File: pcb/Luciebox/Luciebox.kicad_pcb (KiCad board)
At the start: 2 copper layers, 100 x 100 mm, 83 parts, among them J1 Screw_Terminal_01x07, J2 Screw_Terminal_01x07, J3 Screw_Terminal_01x07, J4 Screw_Terminal_01x07, J5 Screw_Terminal_01x07, P1 CONN_01X01, P2 CONN_01X01, P3 CONN_01X01, P4 CONN_01X01, P5 Digital, P6 Power, P7 Digital, P8 Analog, Q1 BC558, Q2 N-Channel_Mosfet, T1 terminal_13x1, T10 terminal_8x1, T11 terminal_3x1, T2 terminal_8x1, T3 terminal_8x1, T4 terminal_8x1, T5 terminal_8x1, T6 terminal_8x1, T7 terminal_8x1, T8 terminal_8x1, T9 terminal_8x1, U1 CA56-12SRWA, U2 ULN2003A, U3 ATmega328-PU, Y1 16MHz

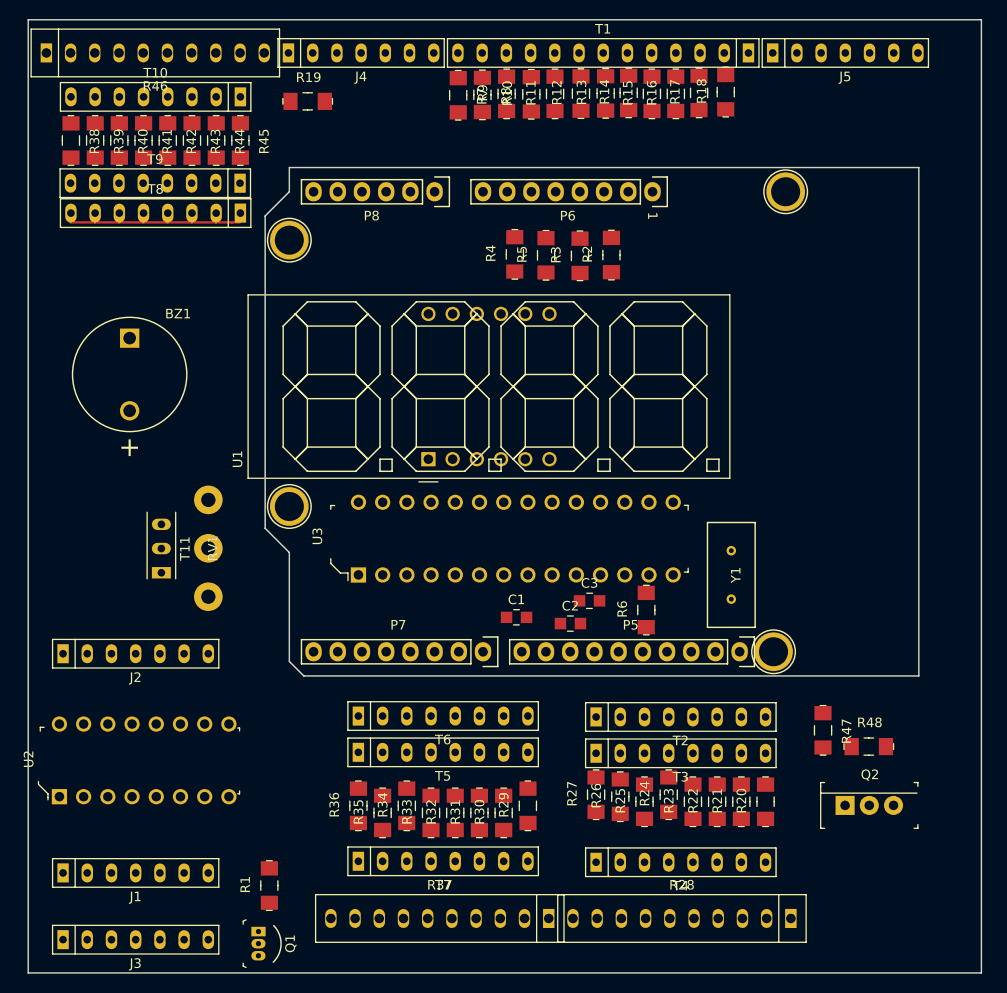
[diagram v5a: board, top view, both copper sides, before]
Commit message: pcb arrange components to input and ouput regions
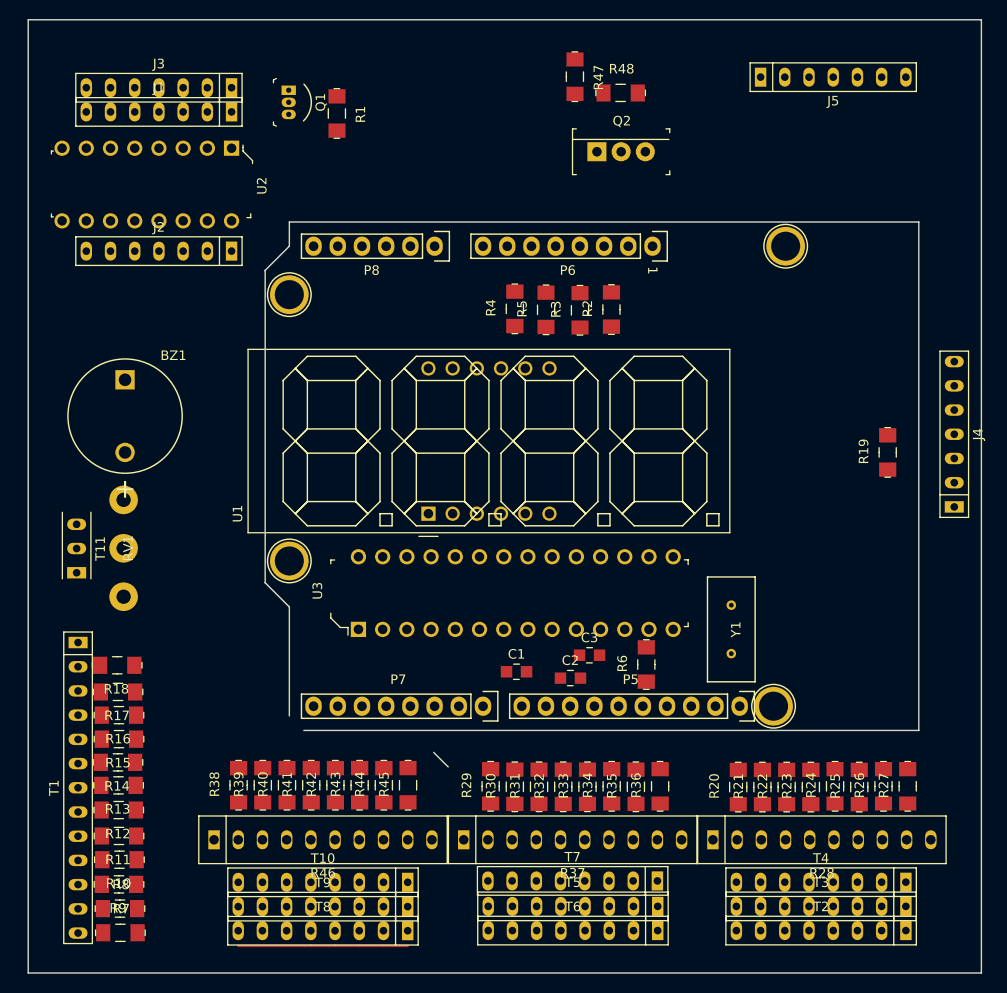
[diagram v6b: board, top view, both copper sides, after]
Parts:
- moved T1 94.8 mm to (85.2, 130.6), turned to 270 degrees
- moved R7 94.7 mm to (89.7, 145.8), turned to 0 degrees
- moved R8 93.5 mm to (89.6, 143.2), turned to 0 degrees
- moved R9 92.4 mm to (89.5, 140.7), turned to 180 degrees
- moved R10 91.2 mm to (89.6, 138.1), turned to 180 degrees
- moved R11 90.3 mm to (89.5, 135.6), turned to 180 degrees
- moved R12 89.5 mm to (89.5, 132.9), turned to 180 degrees
- moved J3 89.4 mm to (93.7, 57.1), turned to 180 degrees
- moved R13 88.8 mm to (89.5, 130.3), turned to 180 degrees
- moved R14 88.3 mm to (89.4, 127.9), turned to 180 degrees
- moved Q1 88.3 mm to (107.3, 57.4)
- moved R15 87.8 mm to (89.5, 125.5), turned to 180 degrees
- moved R18 87.7 mm to (89.3, 117.7), turned to 180 degrees
- moved R17 87.6 mm to (89.4, 120.5), turned to 180 degrees
- moved R16 87.5 mm to (89.5, 123.0), turned to 180 degrees
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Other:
- outline, holes or cut-outs redrawn

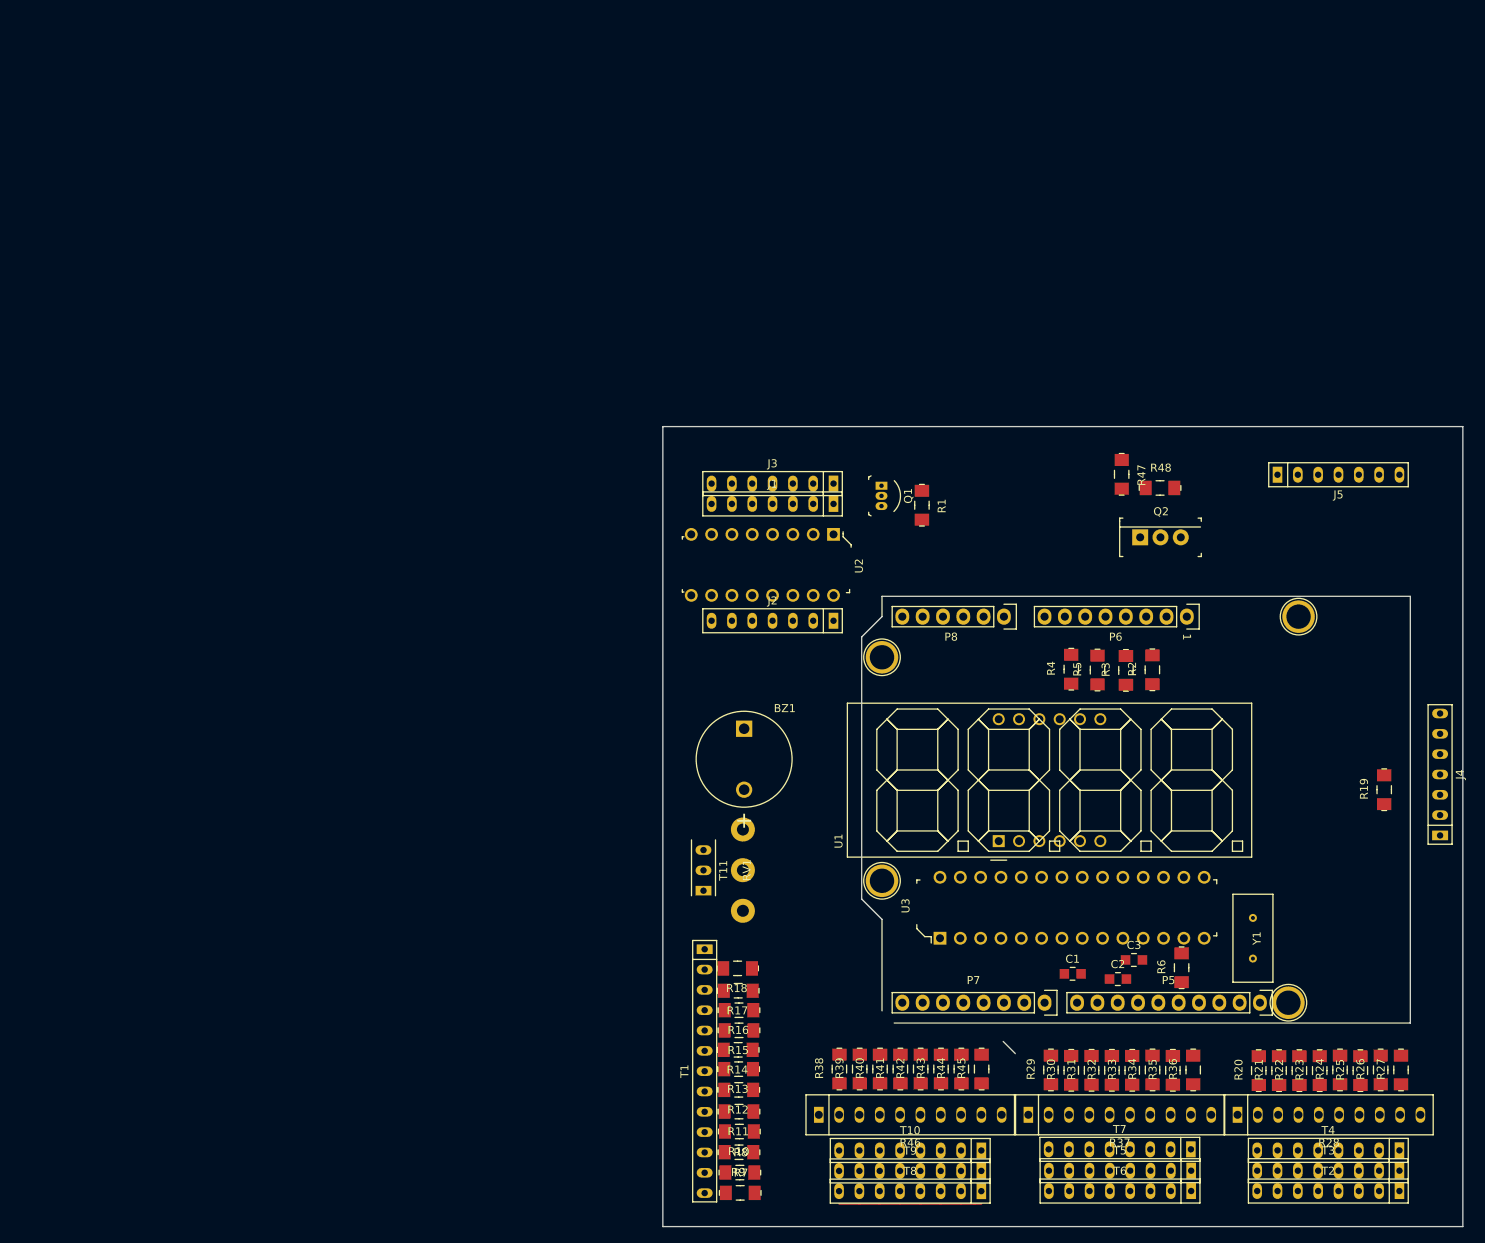
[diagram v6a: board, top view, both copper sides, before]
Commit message: pcb all traces made. Copper pours in place. Check for trace widths and artwork.
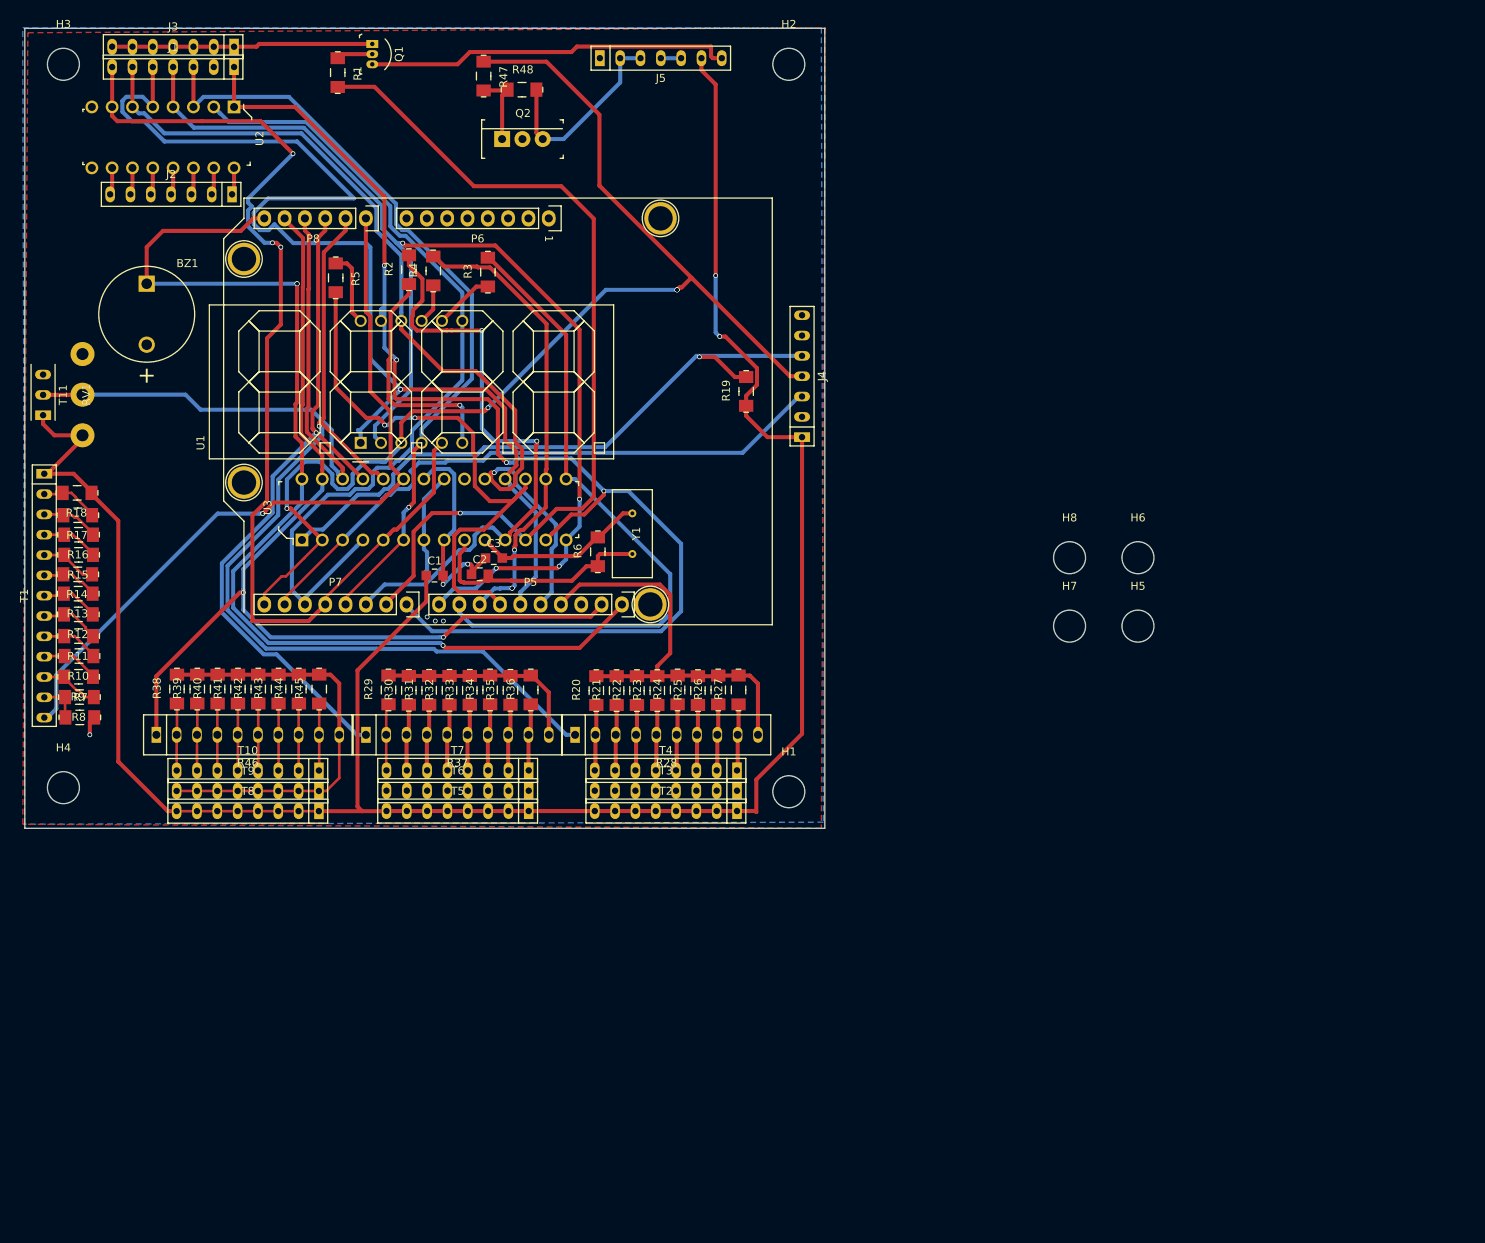
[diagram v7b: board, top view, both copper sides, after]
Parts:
- added H1: MountingHole, MountingHole:MountingHole_4mm, F.Cu at (95.7, 95.6)
- added H2: MountingHole, MountingHole:MountingHole_4mm, F.Cu at (95.7, 4.71)
- added H3: MountingHole, MountingHole:MountingHole_4mm, F.Cu at (5.07, 4.71)
- added H4: MountingHole, MountingHole:MountingHole_4mm, F.Cu at (5.07, 95.1)
- added H5: MountingHole, MountingHole:MountingHole_4mm, F.Cu at (139.4, 74.9)
- added H6: MountingHole, MountingHole:MountingHole_4mm, F.Cu at (139.4, 66.4)
- added H7: MountingHole, MountingHole:MountingHole_4mm, F.Cu at (130.8, 74.9)
- added H8: MountingHole, MountingHole:MountingHole_4mm, F.Cu at (130.8, 66.4)
- moved R5 107.1 mm to (39.1, 31.4), turned to 270 degrees
- moved R2 105.5 mm to (48.2, 30.4)
- moved R7 101.7 mm to (7.12, 86.4)
- moved R8 101.7 mm to (7.08, 83.8), turned to 180 degrees
- moved R10 101.7 mm to (7.02, 78.7)
- moved R11 101.7 mm to (6.97, 76.2)
- moved R12 101.7 mm to (6.94, 73.5)
- moved R13 101.7 mm to (6.92, 70.9)
- moved R14 101.7 mm to (6.87, 68.5)
- moved R15 101.7 mm to (6.97, 66.0)
- moved R16 101.7 mm to (6.97, 63.5)
- moved R17 101.7 mm to (6.87, 61.1)
- moved R18 101.7 mm to (6.79, 58.3)
- moved R9 101.7 mm to (6.97, 81.3)
- moved RV1 101.7 mm to (7.46, 46.0)
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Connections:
- J5 pad 7: Net-(J5-Pad7) -> +12V
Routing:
- net VCC: track 17.8 -> 291.2 mm, vias 0 -> 2
- net GND: track 0.00 -> 164.4 mm, vias 0 -> 6
- net /7: track 0.00 -> 158.5 mm, vias 0 -> 4
- net /0(Rx): track 0.00 -> 149.7 mm, vias 0 -> 5
- net /12(MISO): track 0.00 -> 146.0 mm, vias 0 -> 1
- net /8: track 0.00 -> 144.6 mm, vias 0 -> 4
- net /A5(SCL): track 0.00 -> 137.1 mm, vias 0 -> 3
- net /3(PWM): track 0.00 -> 132.3 mm, vias 0 -> 3
- net /A4(SDA): track 0.00 -> 125.7 mm, vias 0 -> 2
- net /A1: track 0.00 -> 116.1 mm, vias 0 -> 1
- net /13(SCK): track 0.00 -> 113.9 mm, vias 0 -> 1
- net /6(PWM): track 0.00 -> 111.1 mm, vias 0 -> 1
- net /2: track 0.00 -> 105.3 mm
- net /4: track 0.00 -> 97.3 mm, vias 0 -> 1
- net /A0: track 0.00 -> 94.3 mm, vias 0 -> 1
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- added copper zone on B.Cu, net GND
- added copper zone on F.Cu, net GND
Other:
- outline, holes or cut-outs redrawn
- net class Default: trace_width 0.25 -> 0.508
